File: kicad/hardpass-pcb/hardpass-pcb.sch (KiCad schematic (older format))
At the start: 53 parts, among them P1 Pi_Zero, P2 OLED_I2C, P3 Pi_Zero, SW1 1, SW10 C/UP, SW11 0/OK, SW12 OK/DN, SW13 SHUTDN, SW14 SW_PUSH_SMALL, SW2 2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

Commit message: reset circuit redesign WARN: multiple defined@once
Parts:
- added IC?: APX803, symbol CONN_01X03
- added R?: 10k, Resistors_SMD:R_1206, symbol R_Small
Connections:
- net +3V3: now also IC?.3 (P3), R?.1
- net GND: now also IC?.1 (P1)
- net OLED_RST: now reaches P1.12 (P12)
- net OLED_RST: now also P2.14 (P14), R3.1, IC?.2 (P2), R?.2
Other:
- note added: "Changes according to github.com/adafruit/Adafruit-128x64-OLED-Bonnet-for-Raspberry-Pi-PCB: \n * C1, C2, C5, C6: 2.2µF\n * C4: 2.2µF\n * C3: 10µF\n * Reset: APX803(1=GND, 2=OLED_RST, 3=3V3)---(OLED_RST)---10k---3V3\nOther Changes:\n * Pi OLED Software Reset GPIO18 (Pin12)"
- moved on the sheet: C7, R2, R3
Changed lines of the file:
@@
 L C_Small C7
 U 1 1 58337245
-P 4550 2450
-F 0 "C7" H 4600 2400 50  0000 L CNN
-F 1 "0.1µF" H 4300 2400 50  0000 L CNN
-F 2 "Capacitors_SMD:C_1206" H 7150 2450 50  0001 C CNN
-F 3 "" H 4550 2450 50  0000 C CNN
-	1    4550 2450
+P 3550 3100
+F 0 "C7" H 3600 3050 50  0000 L CNN
+F 1 "0.1µF" H 3300 3050 50  0000 L CNN
+F 2 "Capacitors_SMD:C_1206" H 6150 3100 50  0001 C CNN
+F 3 "" H 3550 3100 50  0000 C CNN
+	1    3550 3100
 	1    0    0    -1
 $EndComp
@@
 L R_Small R2
 U 1 1 583372D3
-P 4550 2250
-F 0 "R2" V 4450 2200 50  0000 L CNN
-F 1 "100k" V 4650 2150 50  0000 L CNN
-F 2 "Resistors_SMD:R_1206" H 1950 2250 50  0001 C CNN
-F 3 "" H 4550 2250 50  0000 C CNN
-	1    4550 2250
+P 3550 2900
+F 0 "R2" V 3450 2850 50  0000 L CNN
+F 1 "100k" V 3650 2800 50  0000 L CNN
+F 2 "Resistors_SMD:R_1206" H 950 2900 50  0001 C CNN
+F 3 "" H 3550 2900 50  0000 C CNN
+	1    3550 2900
 	-1   0    0    1
 $EndComp
@@
 L R_Small R3
 U 1 1 58337469
-P 4800 2350
-F 0 "R3" V 4900 2350 50  0000 L CNN
-F 1 "100k" V 4700 2300 50  0000 L CNN
-F 2 "Resistors_SMD:R_1206" V 4800 4700 50  0001 C CNN
-F 3 "" H 4800 2350 50  0000 C CNN
-	1    4800 2350
+P 3800 3000
+F 0 "R3" V 3900 3000 50  0000 L CNN
+F 1 "100k" V 3700 2950 50  0000 L CNN
+F 2 "Resistors_SMD:R_1206" V 3800 5350 50  0001 C CNN
+F 3 "" H 3800 3000 50  0000 C CNN
+	1    3800 3000
 	0    1    1    0
 $EndComp
@@
 L +3.3V #PWR010
 U 1 1 58337E9C
-P 4550 2150
-F 0 "#PWR010" H 4550 2000 50  0001 C CNN
-F 1 "+3.3V" H 4550 2290 50  0001 C CNN
-F 2 "" H 4550 2150 50  0000 C CNN
-F 3 "" H 4550 2150 50  0000 C CNN
-	1    4550 2150
+P 3550 2800
+F 0 "#PWR010" H 3550 2650 50  0001 C CNN
+F 1 "+3.3V" H 3550 2940 50  0001 C CNN
+F 2 "" H 3550 2800 50  0000 C CNN
+F 3 "" H 3550 2800 50  0000 C CNN
+	1    3550 2800
 	1    0    0    -1
 $EndComp
@@
 L GND #PWR011
 U 1 1 58337F0D
-P 4550 2550
-F 0 "#PWR011" H 4550 2300 50  0001 C CNN
-F 1 "GND" H 4550 2400 50  0001 C CNN
-F 2 "" H 4550 2550 50  0000 C CNN
-F 3 "" H 4550 2550 50  0000 C CNN
-	1    4550 2550
+P 3550 3200
+F 0 "#PWR011" H 3550 2950 50  0001 C CNN
+F 1 "GND" H 3550 3050 50  0001 C CNN
+F 2 "" H 3550 3200 50  0000 C CNN
+F 3 "" H 3550 3200 50  0000 C CNN
+	1    3550 3200
 	1    0    0    -1
 $EndComp
@@
 Connection ~ 4950 2700
 Wire Wire Line
-	4700 2350 4550 2350
+	3700 3000 3550 3000
 Wire Wire Line
 	4600 5700 4800 5700
@@
 	8750 2600 8750 2400
 Connection ~ 8750 2400
+Text Notes 2300 1200 0    60   ~ 0
+Changes according to github.com/adafruit/Adafruit-128x64-OLED-Bonnet-for-Raspberry-Pi-PCB: \n * C1, C2, C5, C6: 2.2µF\n * C4: 2.2µF\n * C3: 10µF\n * Reset: APX803(1=GND, 2=OLED_RST, 3=3V3)---(OLED_RST)---10k---3V3\nOther Changes:\n * Pi OLED Software Reset GPIO18 (Pin12)
+Text GLabel 2250 1600 2    60   Input ~ 0
+OLED_RST
+Text GLabel 4900 2350 0    60   Input ~ 0
+OLED_RST
+$Comp
+L CONN_01X03 IC?
+U 1 1 593C6F9B
+P 3650 1550
+F 0 "IC?" H 3650 1750 50  0000 C CNN
+F 1 "APX803" V 3750 1550 50  0000 C CNN
+F 2 "" H 3650 1550 50  0001 C CNN
+F 3 "" H 3650 1550 50  0001 C CNN
+	1    3650 1550
+	0    -1   -1   0
+$EndComp
+$Comp
+L GND #PWR?
+U 1 1 593C7371
+P 3550 1750
+F 0 "#PWR?" H 3550 1500 50  0001 C CNN
+F 1 "GND" H 3550 1600 50  0001 C CNN
+F 2 "" H 3550 1750 50  0000 C CNN
+F 3 "" H 3550 1750 50  0000 C CNN
+	1    3550 1750
+	1    0    0    -1
+$EndComp
+$Comp
+L +3.3V #PWR?
+U 1 1 593C741B
+P 3850 1750
+F 0 "#PWR?" H 3850 1600 50  0001 C CNN
+F 1 "+3.3V" H 3850 1890 50  0001 C CNN
+F 2 "" H 3850 1750 50  0000 C CNN
+F 3 "" H 3850 1750 50  0000 C CNN
+	1    3850 1750
+	1    0    0    -1
+$EndComp
+$Comp
+L R_Small R?
+U 1 1 593C7684
+P 3750 1850
+F 0 "R?" V 3800 1950 50  0000 L CNN
+F 1 "10k" V 3800 1800 50  0000 L CNN
+F 2 "Resistors_SMD:R_1206" V 3750 3350 50  0001 C CNN
+F 3 "" H 3750 1850 50  0000 C CNN
+	1    3750 1850
+	0    1    1    0
+$EndComp
+Wire Wire Line
+	3650 1750 3650 1900
+Wire Wire Line
+	3750 1750 3850 1750
+Wire Wire Line
+	3850 1750 3850 1850
+Text GLabel 3650 1900 3    60   Input ~ 0
+OLED_RST
+Connection ~ 3650 1850
+Text GLabel 3900 3000 3    60   Input ~ 0
+OLED_RST
+Wire Notes Line
+	3350 2600 3350 3550
+Wire Notes Line
+	3350 3550 4000 3550
+Wire Notes Line
+	4000 3550 4000 2600
+Wire Notes Line
+	4000 2600 3350 2600
+Wire Notes Line
+	3350 1350 3350 2450
+Wire Notes Line
+	3350 2450 4000 2450
+Wire Notes Line
+	4000 2450 4000 1350
+Wire Notes Line
+	4000 1350 3350 1350
 $EndSCHEMATC

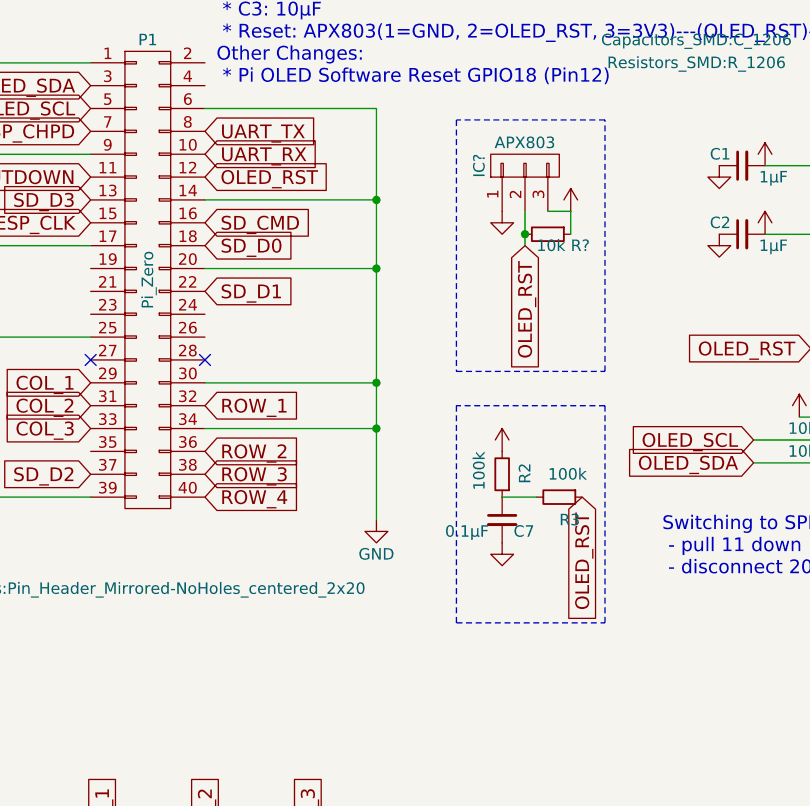
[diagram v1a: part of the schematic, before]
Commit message: remove other non-ic reset methods
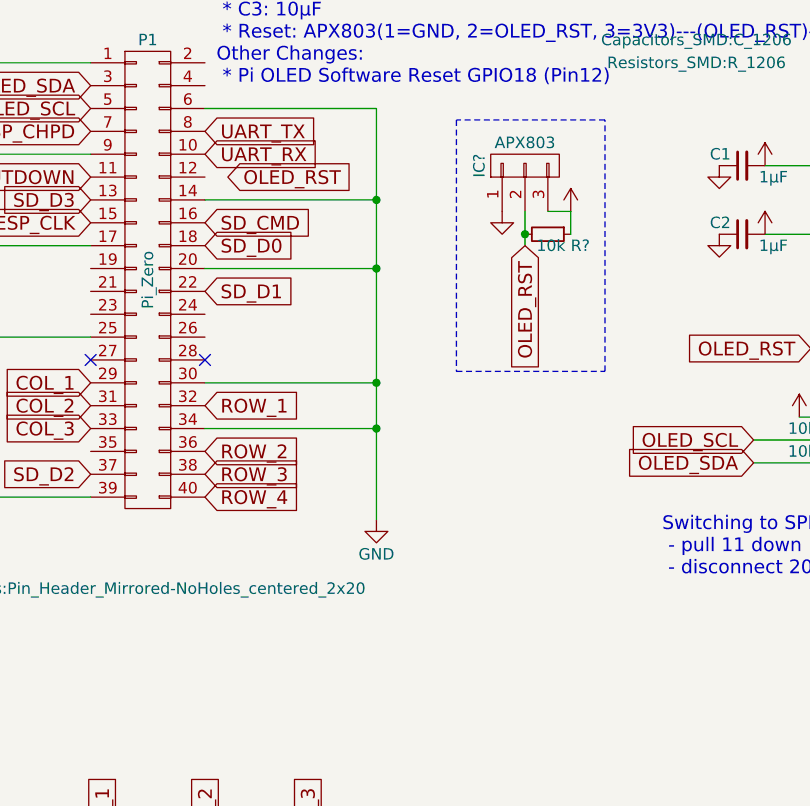
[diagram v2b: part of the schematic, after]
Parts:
- removed C7: 0.1µF, Capacitors_SMD:C_1206, symbol C_Small
- removed R2, R3: 100k, Resistors_SMD:R_1206, symbol R_Small
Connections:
- net OLED_RST: no longer P1.12 (P12)
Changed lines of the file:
@@
-	1    0    0    -1
-$EndComp
-$Comp
-L C_Small C7
-U 1 1 58337245
-P 3550 3100
-F 0 "C7" H 3600 3050 50  0000 L CNN
-F 1 "0.1µF" H 3300 3050 50  0000 L CNN
-F 2 "Capacitors_SMD:C_1206" H 6150 3100 50  0001 C CNN
-F 3 "" H 3550 3100 50  0000 C CNN
-	1    3550 3100
-	1    0    0    -1
-$EndComp
-$Comp
-L R_Small R2
-U 1 1 583372D3
-P 3550 2900
-F 0 "R2" V 3450 2850 50  0000 L CNN
-F 1 "100k" V 3650 2800 50  0000 L CNN
-F 2 "Resistors_SMD:R_1206" H 950 2900 50  0001 C CNN
-F 3 "" H 3550 2900 50  0000 C CNN
-	1    3550 2900
-	-1   0    0    1
-$EndComp
-$Comp
-L R_Small R3
-U 1 1 58337469
-P 3800 3000
-F 0 "R3" V 3900 3000 50  0000 L CNN
-F 1 "100k" V 3700 2950 50  0000 L CNN
-F 2 "Resistors_SMD:R_1206" V 3800 5350 50  0001 C CNN
-F 3 "" H 3800 3000 50  0000 C CNN
-	1    3800 3000
-	0    1    1    0
-$EndComp
-$Comp
-L +3.3V #PWR010
-U 1 1 58337E9C
-P 3550 2800
-F 0 "#PWR010" H 3550 2650 50  0001 C CNN
-F 1 "+3.3V" H 3550 2940 50  0001 C CNN
-F 2 "" H 3550 2800 50  0000 C CNN
-F 3 "" H 3550 2800 50  0000 C CNN
-	1    3550 2800
-	1    0    0    -1
-$EndComp
-$Comp
-L GND #PWR011
-U 1 1 58337F0D
-P 3550 3200
-F 0 "#PWR011" H 3550 2950 50  0001 C CNN
-F 1 "GND" H 3550 3050 50  0001 C CNN
-F 2 "" H 3550 3200 50  0000 C CNN
-F 3 "" H 3550 3200 50  0000 C CNN
-	1    3550 3200
 	1    0    0    -1
 $EndComp
@@
 Connection ~ 4950 2700
 Wire Wire Line
-	3700 3000 3550 3000
-Wire Wire Line
 	4600 5700 4800 5700
 Wire Wire Line
@@
 Text Notes 2300 1200 0    60   ~ 0
 Changes according to github.com/adafruit/Adafruit-128x64-OLED-Bonnet-for-Raspberry-Pi-PCB: \n * C1, C2, C5, C6: 2.2µF\n * C4: 2.2µF\n * C3: 10µF\n * Reset: APX803(1=GND, 2=OLED_RST, 3=3V3)---(OLED_RST)---10k---3V3\nOther Changes:\n * Pi OLED Software Reset GPIO18 (Pin12)
-Text GLabel 2250 1600 2    60   Input ~ 0
+Text GLabel 2350 1600 2    60   Input ~ 0
 OLED_RST
 Text GLabel 4900 2350 0    60   Input ~ 0
@@
 OLED_RST
 Connection ~ 3650 1850
-Text GLabel 3900 3000 3    60   Input ~ 0
-OLED_RST
-Wire Notes Line
-	3350 2600 3350 3550
-Wire Notes Line
-	3350 3550 4000 3550
-Wire Notes Line
-	4000 3550 4000 2600
-Wire Notes Line
-	4000 2600 3350 2600
 Wire Notes Line
 	3350 1350 3350 2450

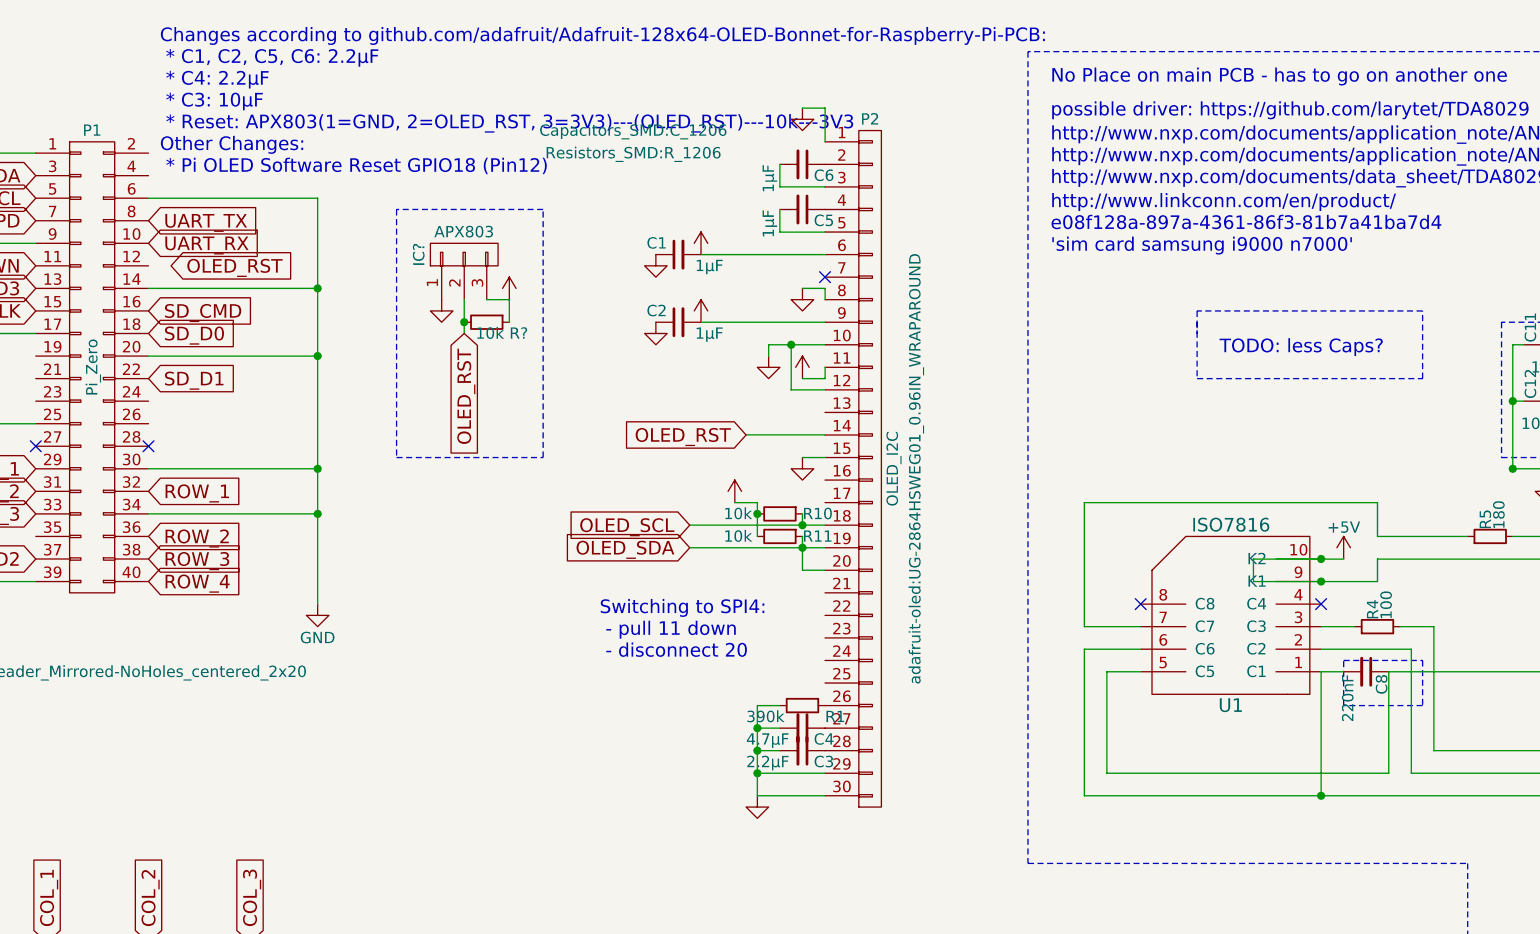
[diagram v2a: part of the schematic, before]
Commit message: reset circuit works; cleanup on it
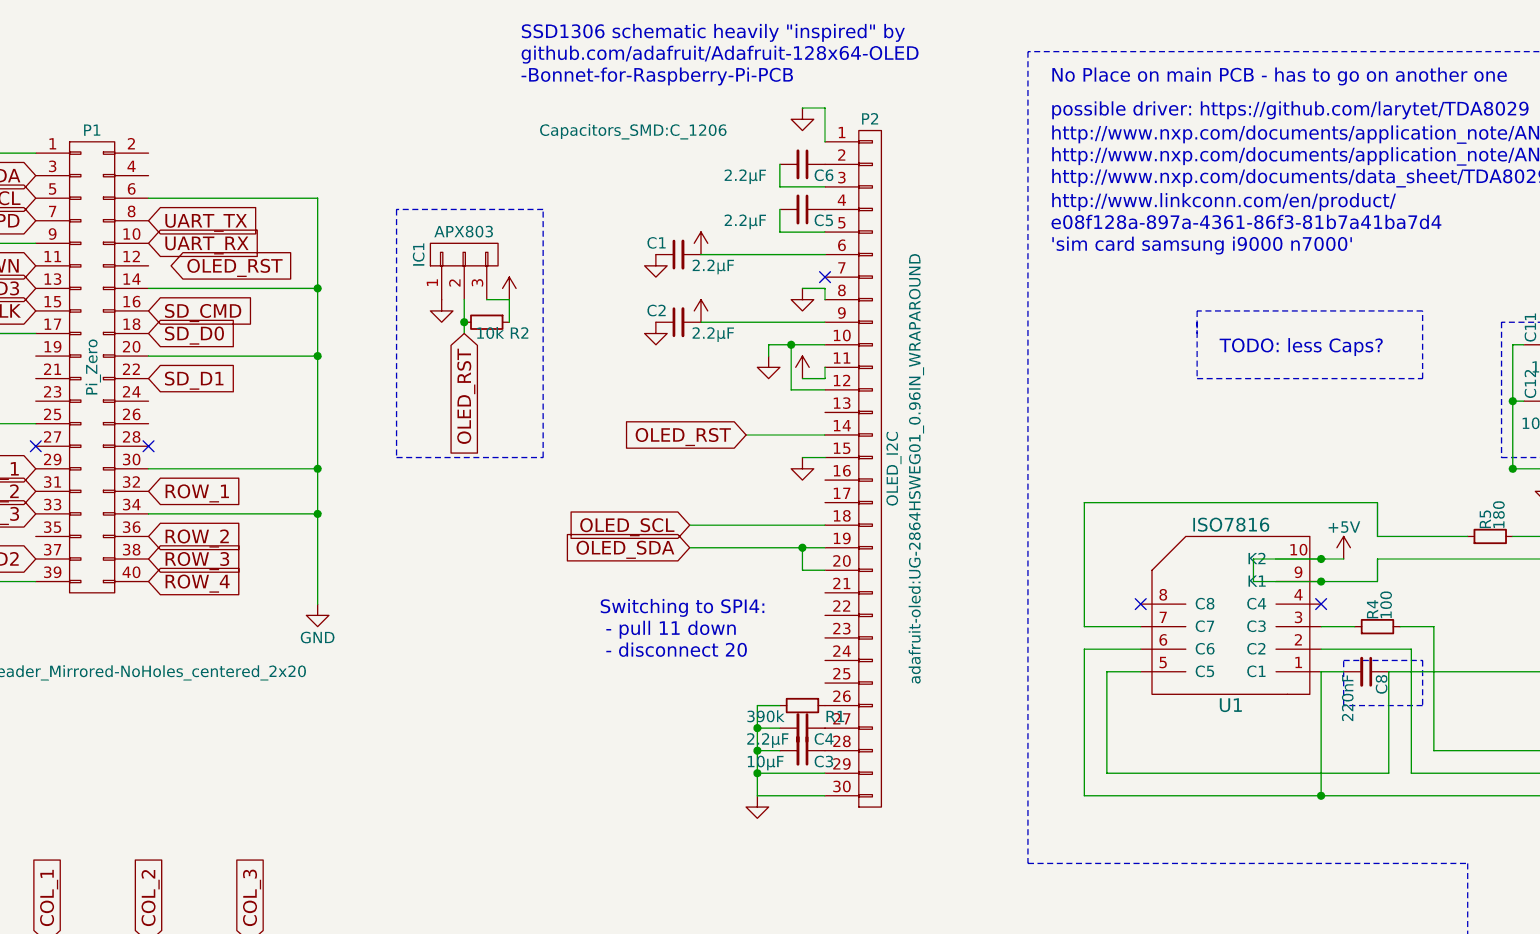
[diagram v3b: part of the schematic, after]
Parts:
- removed R10, R11: 10k, Resistors_SMD:R_1206, symbol R_Small
- C1, C2, C5, C6: value 1µF -> 2.2µF
- C3: value 2.2µF -> 10µF
- C4: value 4.7µF -> 2.2µF
- IC1: renamed from IC?; footprint (none) -> TO_SOT_Packages_SMD:SOT-23
- gave numbers to parts that had none: 1
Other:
- note added: "SSD1306 schematic heavily "inspired" by\ngithub.com/adafruit/Adafruit-128x64-OLED\n-Bonnet-for-Raspberry-Pi-PCB"
- note removed: "Changes according to github.com/adafruit/Adafruit-128x64-OLED-Bonnet-for-Raspberry-Pi-PCB: \n * C1, C2, C5, C6: 2.2µF\n * C4: 2.2µF\n * C3: 10µF\n * Reset: APX803(1=GND, 2=OLED_RST, 3=3V3)---(OLED_RST)---10k---3V3\nOther Changes:\n * Pi OLED Software Reset GPIO18 (Pin12)"
